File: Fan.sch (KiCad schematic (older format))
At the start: 9 parts

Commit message: arduino module / hooking things up
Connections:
- net labels added: CURR_MEAS, FAN_EN_N, FAN_OUT+, FAN_OUT-, TACH_IN, TACH_MEAS
- net labels removed: Current Measure, Fan_In, Power+, Power-, Tach, Tach_Out
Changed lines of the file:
@@
 $EndDescr
 Text HLabel 6900 3100 2    60   Output ~ 0
-Power+
-Text HLabel 6900 3450 2    60   Input ~ 0
-Power-
+FAN_OUT+
+Text HLabel 6900 3450 2    60   Output ~ 0
+FAN_OUT-
 Text HLabel 6900 3800 2    60   Input ~ 0
-Tach
+TACH_IN
 Text HLabel 1350 4250 0    60   Output ~ 0
-Tach_Out
+TACH_MEAS
 Text HLabel 1350 3750 0    60   Input ~ 0
-Fan_In
+FAN_EN_N
 $Comp
 L LM293 U?
@@
 	3700 3400 3700 3550
 Text HLabel 1350 4000 0    60   Output ~ 0
-Current Measure
+CURR_MEAS
 Wire Wire Line
 	6000 3600 5750 3600

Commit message: currentfan revisited
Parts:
- removed R? (x3): R, ~, symbol R
- removed RV?: POT, ~, symbol POT
- added D?: DIODE, ~, symbol DIODE
- added Q? (x2): MOSFET_N, ~, symbol MOSFET_N
- added TH?: THERMISTOR, ~, symbol THERMISTOR
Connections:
- net labels added: +12C, FAN_MODE, FAN_PWM_N
- net labels removed: +5V, FAN_EN_N
- wire segments 37 -> 36
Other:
- moved on the sheet: Q?, R?, U?, U?A

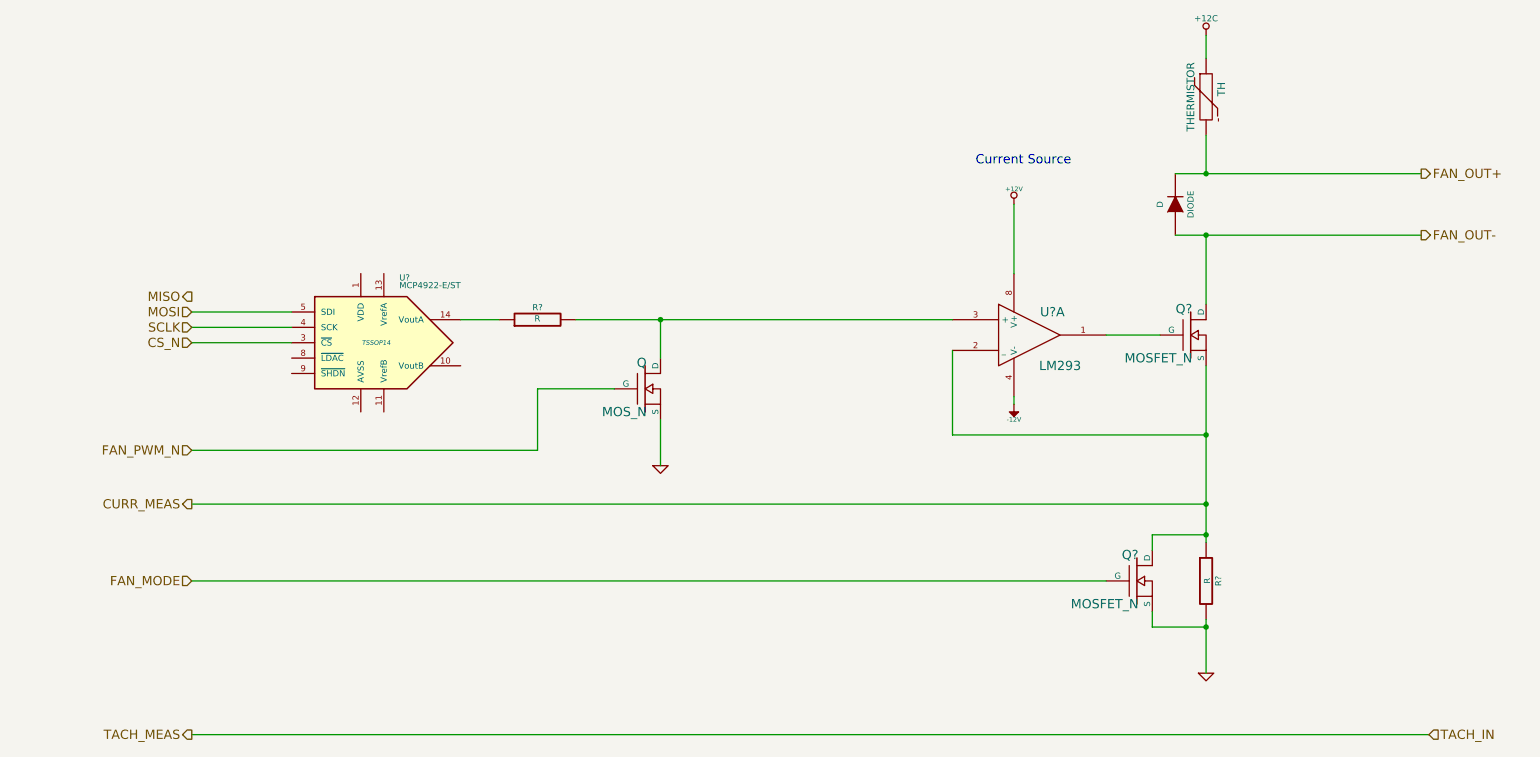
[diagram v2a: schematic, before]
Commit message: associating and placing relay module
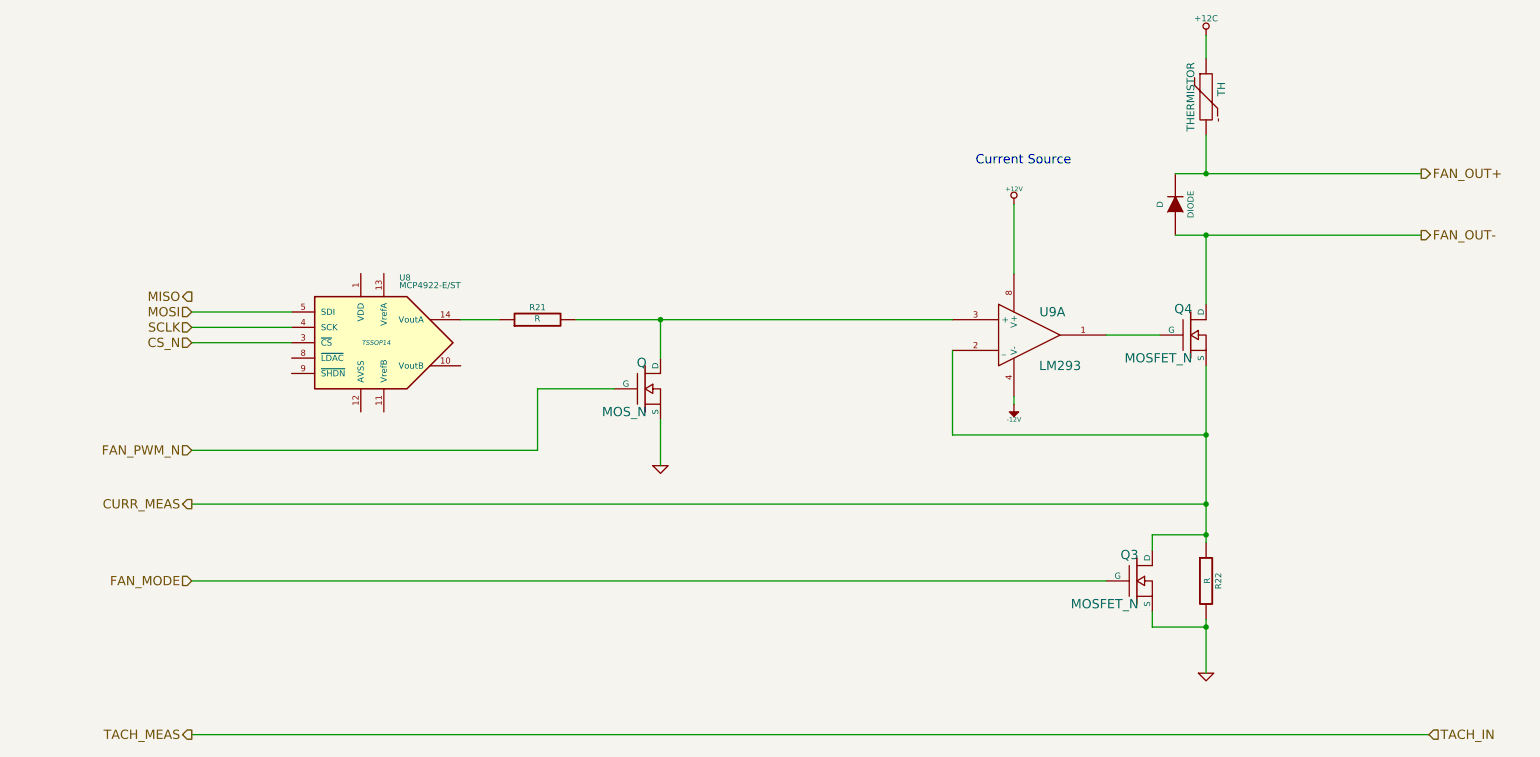
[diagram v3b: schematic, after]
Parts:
- gave numbers to parts that had none: 9
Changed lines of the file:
@@
 Sheet 8 9
 Title ""
-Date "10 feb 2014"
+Date "22 feb 2014"
 Rev ""
 Comp ""
@@
 FAN_PWM_N
 $Comp
-L LM293 U?
+L LM293 U9
 U 1 1 52F10F8D
 P 7000 3200
-F 0 "U?" H 7150 3350 60  0000 C CNN
+F 0 "U9" H 7150 3350 60  0000 C CNN
 F 1 "LM293" H 7200 3000 60  0000 C CNN
 F 2 "" H 7000 3200 60  0000 C CNN
@@
 $EndComp
 $Comp
-L R R?
+L R R22
 U 1 1 52F10F9C
 P 8150 4800
-F 0 "R?" V 8230 4800 40  0000 C CNN
+F 0 "R22" V 8230 4800 40  0000 C CNN
 F 1 "R" V 8157 4801 40  0000 C CNN
 F 2 "~" V 8080 4800 30  0000 C CNN
@@
 $EndComp
 $Comp
-L +12V #PWR?
+L +12V #PWR044
 U 1 1 52F11039
 P 6900 2350
-F 0 "#PWR?" H 6900 2300 20  0001 C CNN
+F 0 "#PWR044" H 6900 2300 20  0001 C CNN
 F 1 "+12V" H 6900 2450 30  0000 C CNN
 F 2 "" H 6900 2350 60  0000 C CNN
@@
 $EndComp
 $Comp
-L GND #PWR?
+L GND #PWR045
 U 1 1 52F11C1B
 P 4600 4050
-F 0 "#PWR?" H 4600 4050 30  0001 C CNN
+F 0 "#PWR045" H 4600 4050 30  0001 C CNN
 F 1 "GND" H 4600 3980 30  0001 C CNN
 F 2 "" H 4600 4050 60  0000 C CNN
@@
 Current Source
 $Comp
-L MOSFET_N Q?
+L MOSFET_N Q4
 U 1 1 52F36CCA
 P 8050 3200
-F 0 "Q?" H 8060 3370 60  0000 R CNN
+F 0 "Q4" H 8060 3370 60  0000 R CNN
 F 1 "MOSFET_N" H 8060 3050 60  0000 R CNN
 F 2 "~" H 8050 3200 60  0000 C CNN
@@
 $EndComp
 $Comp
-L -12V #PWR?
+L -12V #PWR046
 U 1 1 52F36D24
 P 6900 3650
-F 0 "#PWR?" H 6900 3780 20  0001 C CNN
+F 0 "#PWR046" H 6900 3780 20  0001 C CNN
 F 1 "-12V" H 6900 3750 30  0000 C CNN
 F 2 "" H 6900 3650 60  0000 C CNN
@@
 $EndComp
 $Comp
-L GND #PWR?
+L GND #PWR047
 U 1 1 52F36D47
 P 8150 5400
-F 0 "#PWR?" H 8150 5400 30  0001 C CNN
+F 0 "#PWR047" H 8150 5400 30  0001 C CNN
 F 1 "GND" H 8150 5330 30  0001 C CNN
 F 2 "" H 8150 5400 60  0000 C CNN
@@
 $EndComp
 $Comp
-L MCP4922-E/ST U?
+L MCP4922-E/ST U8
 U 1 1 52F36DAD
 P 2750 3250
-F 0 "U?" H 2900 3650 40  0000 L BNN
+F 0 "U8" H 2900 3650 40  0000 L BNN
 F 1 "MCP4922-E/ST" H 2900 3600 40  0000 L BNN
 F 2 "TSSOP14" H 2750 3250 30  0000 C CIN
@@
 SCLK
 $Comp
-L R R?
+L R R21
 U 1 1 52F36F5D
 P 3800 3100
-F 0 "R?" V 3880 3100 40  0000 C CNN
+F 0 "R21" V 3880 3100 40  0000 C CNN
 F 1 "R" V 3807 3101 40  0000 C CNN
 F 2 "~" V 3730 3100 30  0000 C CNN
@@
 $EndComp
 $Comp
-L MOSFET_N Q?
+L MOSFET_N Q3
 U 1 1 52F8F2F2
 P 7700 4800
-F 0 "Q?" H 7710 4970 60  0000 R CNN
+F 0 "Q3" H 7710 4970 60  0000 R CNN
 F 1 "MOSFET_N" H 7710 4650 60  0000 R CNN
 F 2 "~" H 7700 4800 60  0000 C CNN
@@
 $EndComp
 $Comp
-L THERMISTOR TH?
+L THERMISTOR TH5
 U 1 1 52F8F352
 P 8150 1650
-F 0 "TH?" H 8200 1700 60  0001 C CNN
+F 0 "TH5" H 8200 1700 60  0001 C CNN
 F 1 "THERMISTOR" H 8150 1650 60  0001 C CNN
 F 2 "~" H 8150 1650 60  0000 C CNN
@@
 $EndComp
 $Comp
-L DIODE D?
+L DIODE D5
 U 1 1 52F8F3B9
 P 7950 2350
-F 0 "D?" H 8000 2400 60  0001 C CNN
+F 0 "D5" H 8000 2400 60  0001 C CNN
 F 1 "DIODE" H 7950 2350 60  0001 C CNN
 F 2 "~" H 7950 2350 60  0000 C CNN
@@
 	7850 3200 7500 3200
 Wire Wire Line
-	8150 3400 8150 3850
-Wire Wire Line
-	8150 3850 8150 4300
-Wire Wire Line
-	8150 4300 8150 4500
-Wire Wire Line
-	8150 4500 8150 4550
+	8150 3400 8150 4550
 Wire Wire Line
 	6500 3300 6500 3850
@@
 	6900 3650 6900 3600
 Wire Wire Line
-	8150 5050 8150 5100
-Wire Wire Line
-	8150 5100 8150 5400
-Wire Wire Line
-	4050 3100 4600 3100
-Wire Wire Line
-	4600 3100 6500 3100
+	8150 5050 8150 5400
+Wire Wire Line
+	4050 3100 6500 3100
 Wire Wire Line
 	4600 3750 4600 4050
@@
 	8150 1900 8150 2150
 Wire Wire Line
-	7950 2150 8150 2150
-Wire Wire Line
-	8150 2150 9550 2150
+	7950 2150 9550 2150
 Wire Wire Line
 	8150 3000 8150 2550
 Wire Wire Line
-	7950 2550 8150 2550
-Wire Wire Line
-	8150 2550 9550 2550
+	7950 2550 9550 2550
 Connection ~ 8150 2150
 Connection ~ 8150 2550
@@
 	1550 5800 9600 5800
 $Comp
-L MOSFET_N Q?
+L MOSFET_N Q2
 U 1 1 52F8F4F2
 P 4500 3550
-F 0 "Q?" H 4550 3600 60  0001 C CNN
+F 0 "Q2" H 4550 3600 60  0001 C CNN
 F 1 "MOSFET_N" H 4500 3550 60  0001 C CNN
 F 2 "~" H 4500 3550 60  0000 C CNN
@@
 	7500 4800 1550 4800
 $Comp
-L +12C #PWR?
+L +12C #PWR048
 U 1 1 52F8FBE9
 P 8150 1250
-F 0 "#PWR?" H 8200 1300 60  0001 C CNN
+F 0 "#PWR048" H 8200 1300 60  0001 C CNN
 F 1 "+12C" H 8150 1250 60  0001 C CNN
 F 2 "" H 8150 1250 60  0000 C CNN

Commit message: associating-and-placing-the-thermocouple-module
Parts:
- U8: footprint TSSOP14 -> (none)
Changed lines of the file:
@@
 Sheet 8 9
 Title ""
-Date "22 feb 2014"
+Date "23 feb 2014"
 Rev ""
 Comp ""
@@
 $EndComp
 $Comp
-L +12V #PWR044
+L +12V #PWR051
 U 1 1 52F11039
 P 6900 2350
-F 0 "#PWR044" H 6900 2300 20  0001 C CNN
+F 0 "#PWR051" H 6900 2300 20  0001 C CNN
 F 1 "+12V" H 6900 2450 30  0000 C CNN
 F 2 "" H 6900 2350 60  0000 C CNN
@@
 $EndComp
 $Comp
-L GND #PWR045
+L GND #PWR052
 U 1 1 52F11C1B
 P 4600 4050
-F 0 "#PWR045" H 4600 4050 30  0001 C CNN
+F 0 "#PWR052" H 4600 4050 30  0001 C CNN
 F 1 "GND" H 4600 3980 30  0001 C CNN
 F 2 "" H 4600 4050 60  0000 C CNN
@@
 $EndComp
 $Comp
-L -12V #PWR046
+L -12V #PWR053
 U 1 1 52F36D24
 P 6900 3650
-F 0 "#PWR046" H 6900 3780 20  0001 C CNN
+F 0 "#PWR053" H 6900 3780 20  0001 C CNN
 F 1 "-12V" H 6900 3750 30  0000 C CNN
 F 2 "" H 6900 3650 60  0000 C CNN
@@
 $EndComp
 $Comp
-L GND #PWR047
+L GND #PWR054
 U 1 1 52F36D47
 P 8150 5400
-F 0 "#PWR047" H 8150 5400 30  0001 C CNN
+F 0 "#PWR054" H 8150 5400 30  0001 C CNN
 F 1 "GND" H 8150 5330 30  0001 C CNN
 F 2 "" H 8150 5400 60  0000 C CNN
@@
 F 0 "U8" H 2900 3650 40  0000 L BNN
 F 1 "MCP4922-E/ST" H 2900 3600 40  0000 L BNN
-F 2 "TSSOP14" H 2750 3250 30  0000 C CIN
+F 2 "" H 2750 3250 30  0000 C CIN
 F 3 "" H 2750 3250 60  0000 C CNN
 	1    2750 3250
@@
 	7500 4800 1550 4800
 $Comp
-L +12C #PWR048
+L +12C #PWR055
 U 1 1 52F8FBE9
 P 8150 1250
-F 0 "#PWR048" H 8200 1300 60  0001 C CNN
+F 0 "#PWR055" H 8200 1300 60  0001 C CNN
 F 1 "+12C" H 8150 1250 60  0001 C CNN
 F 2 "" H 8150 1250 60  0000 C CNN

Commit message: fan module
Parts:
- removed Q3, Q4: MOSFET_N, ~, symbol MOSFET_N
- removed U8: MCP4922-E/ST, symbol MCP4922-E/ST
- added C13, C14: C, ~, symbol C
- added Q3, Q4: AOD476, ~, symbol MOS_N_1
- added U8: MCP4801, symbol MCP4801
- D5: value DIODE -> B130-13-F; Distributor (none) -> DigiKey; Distributor Link (none) -> http://www.digikey.com/product-detail/en/B130-13-F/B130-FDI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; Distributor Part Number (none) -> B130-FDICT-ND; MFG Name (none) -> Diodes Inc; MFG Part Number (none) -> B130-13-F; Reference D -> (none); Value DIODE -> (none)
- Q2: value MOSFET_N -> DMN65D8L-7; Distributor (none) -> DigiKey; Distributor Link (none) -> http://www.digikey.com/product-detail/en/DMN65D8L-7/DMN65D8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; Distributor Part Number (none) -> DMN65D8L-7DICT-ND; MFG Name (none) -> Diodes Inc; MFG Part Number (none) -> DMN65D8L-7; Reference Q -> (none); Value MOS_N -> (none)
- R22: value R -> 1
- TH5: value THERMISTOR -> PTC 500mA; Distributor (none) -> DigiKey; Distributor Link (none) -> http://www.digikey.com/product-detail/en/MINISMDC050F-2/MIN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; Distributor Part Number (none) -> MINISMDC050FCT-ND; MFG Name (none) -> TE Connectivity; MFG Part Number (none) -> MINISMDC050F-2; Reference TH -> (none); Value THERMISTOR -> (none)
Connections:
- net +12C: now also C14.2
- net CS_N: now also U8.2 (~CS)
- net CURR_MEAS: now also Q3.2 (D), Q4.3 (S)
- net FAN_MODE: now also Q3.1 (G)
- net FAN_OUT-: now also Q4.2 (D)
- net MOSI: now also U8.4 (SDI)
- net SCLK: now also U8.3 (SCK)
- net at U9.1: now also Q4.1 (G)
- net at R21.1: now also U8.8 (Vout)
- net GND renamed AGND
- net AGND: now also C13.1, C14.1, Q3.3 (S), U8.7 (Vss)
- new net +5V: C13.2, U8.1 (Vdd)
- new net ~LDAC: U8.5 (~LDAC)
- new net ~SHDN: U8.6 (~SHDN)
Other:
- note added: "should this be a different ground?\n"
